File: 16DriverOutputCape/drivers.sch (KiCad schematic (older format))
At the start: 14 parts, among them P1 0 1 2, P2 C A0 A1 A2 A3 A4 A5 A6 A7, P3 C B0 B1 B2 B3 B4 B5 B6 B7, U1 MCP23017, U2 TBD62X83A, U3 TBD62X83A

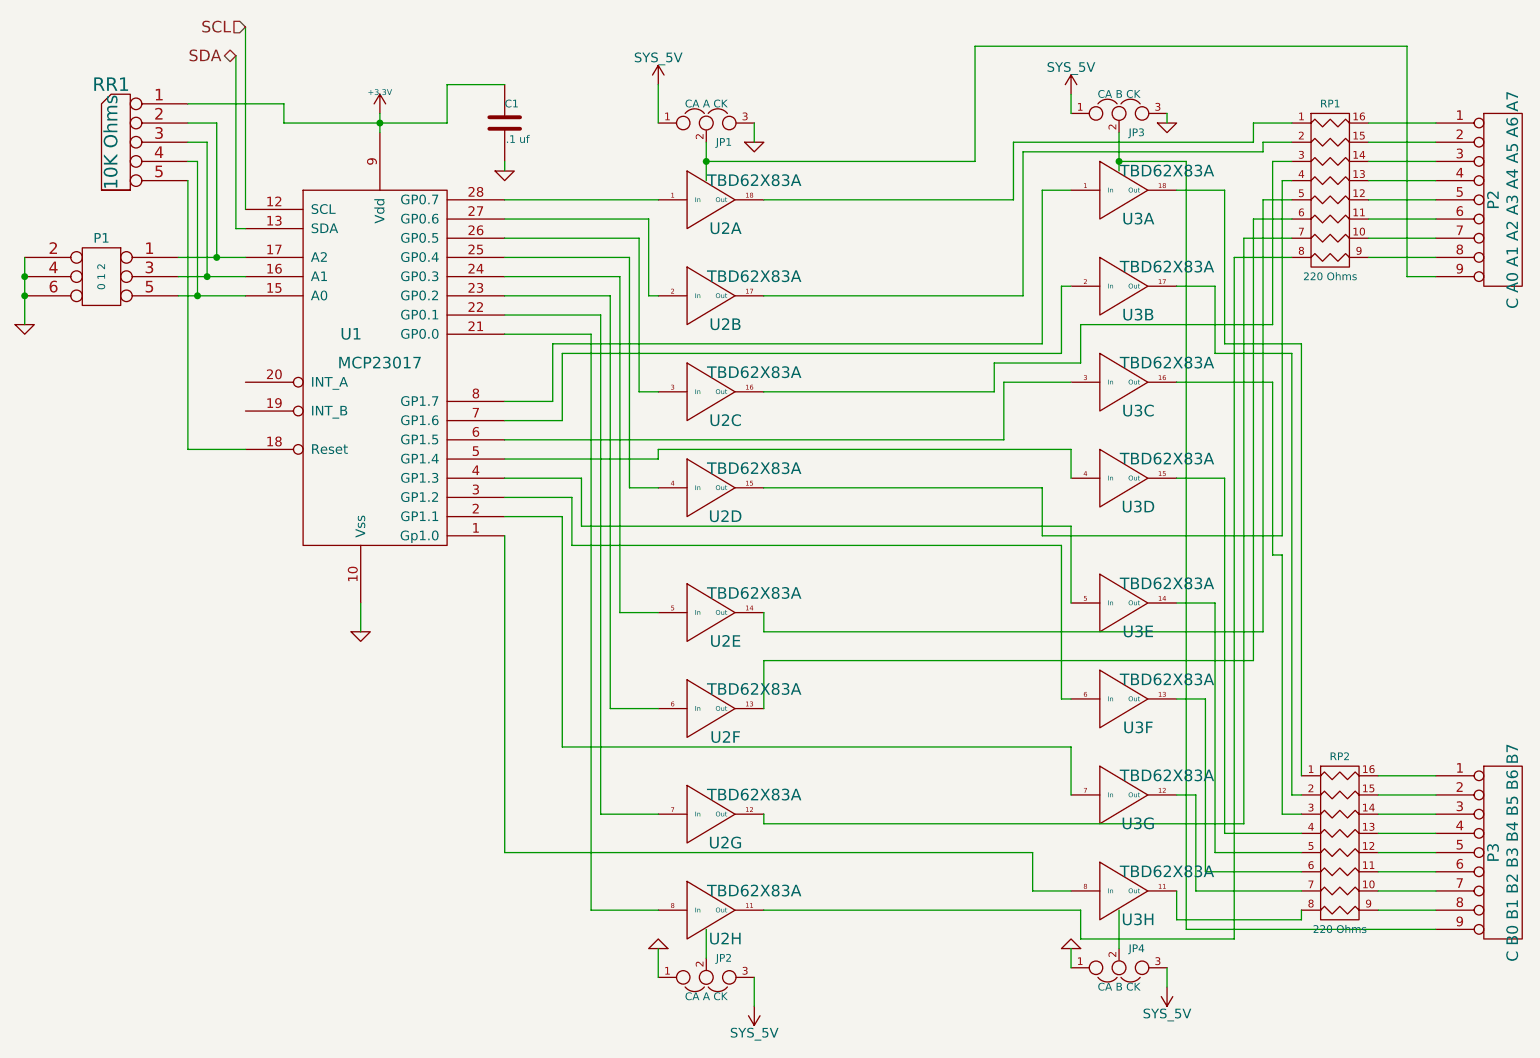
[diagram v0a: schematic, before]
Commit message: Update 16DriverOutputCape to use 12V for the LEDs.
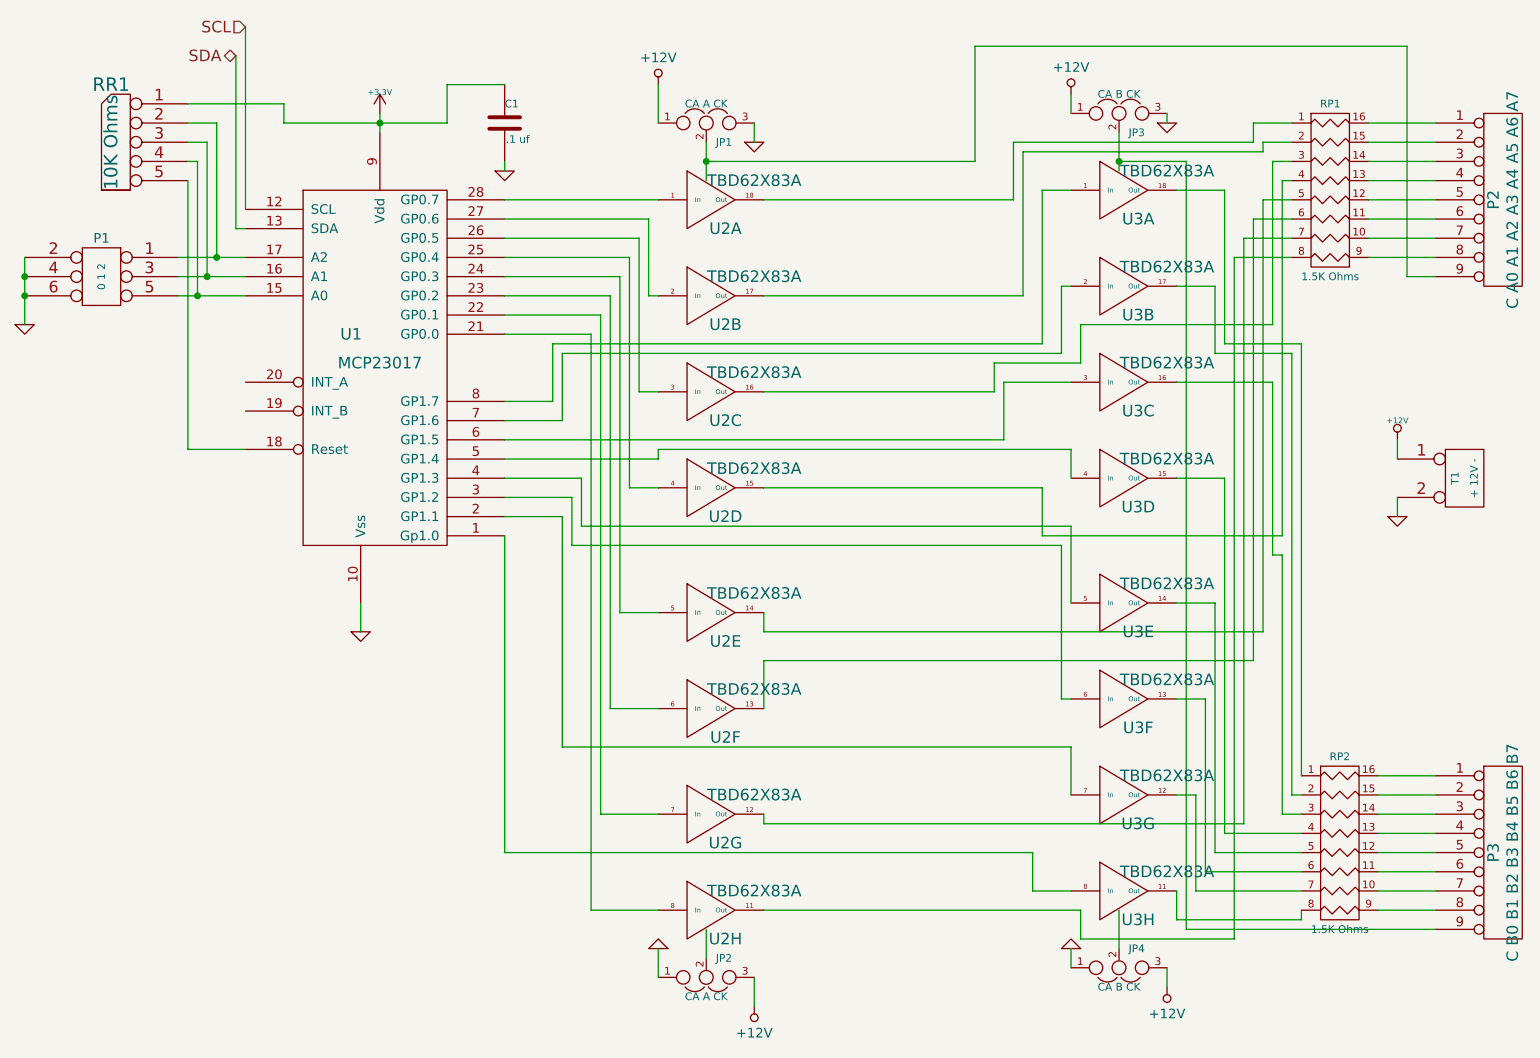
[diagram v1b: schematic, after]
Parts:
- added T1: + 12V -, symbol CONN_2
- RP1, RP2: value 220 Ohms -> 1.5K Ohms
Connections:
- net GND: now also T1.2 (PM)
- net SYS_5V renamed +12V
- net +12V: now also T1.1 (P1)
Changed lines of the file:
@@
 Sheet 2 2
 Title ""
-Date "25 feb 2019"
+Date "28 mar 2019"
 Rev ""
 Comp ""
@@
 P 9900 1500
 F 0 "RP1" H 9900 1950 40  0000 C CNN
-F 1 "220 Ohms" H 9900 1050 40  0000 C CNN
+F 1 "1.5K Ohms" H 9900 1050 40  0000 C CNN
 F 2 "~" H 9900 1500 60  0000 C CNN
 F 3 "~" H 9900 1500 60  0000 C CNN
@@
 P 9950 4900
 F 0 "RP2" H 9950 5350 40  0000 C CNN
-F 1 "220 Ohms" H 9950 4450 40  0000 C CNN
+F 1 "1.5K Ohms" H 9950 4450 40  0000 C CNN
 F 2 "~" H 9950 4900 60  0000 C CNN
 F 3 "~" H 9950 4900 60  0000 C CNN
@@
 SCL
 $Comp
-L SYS_5V #PWR023
+L +12V #PWR023
 U 1 1 5C740255
 P 6400 950
 F 0 "#PWR023" H 6400 800 50  0001 C CNN
-F 1 "SYS_5V" H 6400 1090 50  0000 C CNN
+F 1 "+12V" H 6400 1090 50  0000 C CNN
 F 2 "~" H 6400 950 60  0000 C CNN
 F 3 "~" H 6400 950 60  0000 C CNN
@@
 $EndComp
 $Comp
-L SYS_5V #PWR024
+L +12V #PWR024
 U 1 1 5C740264
 P 8550 1000
 F 0 "#PWR024" H 8550 850 50  0001 C CNN
-F 1 "SYS_5V" H 8550 1140 50  0000 C CNN
+F 1 "+12V" H 8550 1140 50  0000 C CNN
 F 2 "~" H 8550 1000 60  0000 C CNN
 F 3 "~" H 8550 1000 60  0000 C CNN
@@
 $EndComp
 $Comp
-L SYS_5V #PWR025
+L +12V #PWR025
 U 1 1 5C740273
 P 6900 5750
 F 0 "#PWR025" H 6900 5600 50  0001 C CNN
-F 1 "SYS_5V" H 6900 5890 50  0000 C CNN
+F 1 "+12V" H 6900 5890 50  0000 C CNN
 F 2 "~" H 6900 5750 60  0000 C CNN
 F 3 "~" H 6900 5750 60  0000 C CNN
@@
 $EndComp
 $Comp
-L SYS_5V #PWR026
+L +12V #PWR026
 U 1 1 5C740282
 P 9050 5650
 F 0 "#PWR026" H 9050 5500 50  0001 C CNN
-F 1 "SYS_5V" H 9050 5790 50  0000 C CNN
+F 1 "+12V" H 9050 5790 50  0000 C CNN
 F 2 "~" H 9050 5650 60  0000 C CNN
 F 3 "~" H 9050 5650 60  0000 C CNN
@@
 $EndComp
 Connection ~ 3100 2050
+$Comp
+L CONN_2 T1
+U 1 1 5C9C2190
+P 10600 3000
+F 0 "T1" V 10550 3000 40  0000 C CNN
+F 1 "+ 12V -" V 10650 3000 40  0000 C CNN
+F 2 "" H 10600 3000 60  0000 C CNN
+F 3 "" H 10600 3000 60  0000 C CNN
+	1    10600 3000
+	1    0    0    -1
+$EndComp
+$Comp
+L +12V #PWR028
+U 1 1 5C9C21B7
+P 10250 2800
+F 0 "#PWR028" H 10250 2750 20  0001 C CNN
+F 1 "+12V" H 10250 2900 30  0000 C CNN
+F 2 "" H 10250 2800 60  0000 C CNN
+F 3 "" H 10250 2800 60  0000 C CNN
+	1    10250 2800
+	1    0    0    -1
+$EndComp
+$Comp
+L GND #PWR029
+U 1 1 5C9C21C6
+P 10250 3200
+F 0 "#PWR029" H 10250 3200 30  0001 C CNN
+F 1 "GND" H 10250 3130 30  0001 C CNN
+F 2 "" H 10250 3200 60  0000 C CNN
+F 3 "" H 10250 3200 60  0000 C CNN
+	1    10250 3200
+	1    0    0    -1
+$EndComp
+Wire Wire Line
+	10250 2800 10250 2900
+Wire Wire Line
+	10250 3100 10250 3200
 $EndSCHEMATC
